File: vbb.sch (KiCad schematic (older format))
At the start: 24 parts, among them CON1 BARREL_JACK, J1 Screw_Terminal_1x02, P1 CONN_02X01, P3 CONN_02X04, P4 USB_B, P5 USB_B, P6 USB_B, P7 USB_A

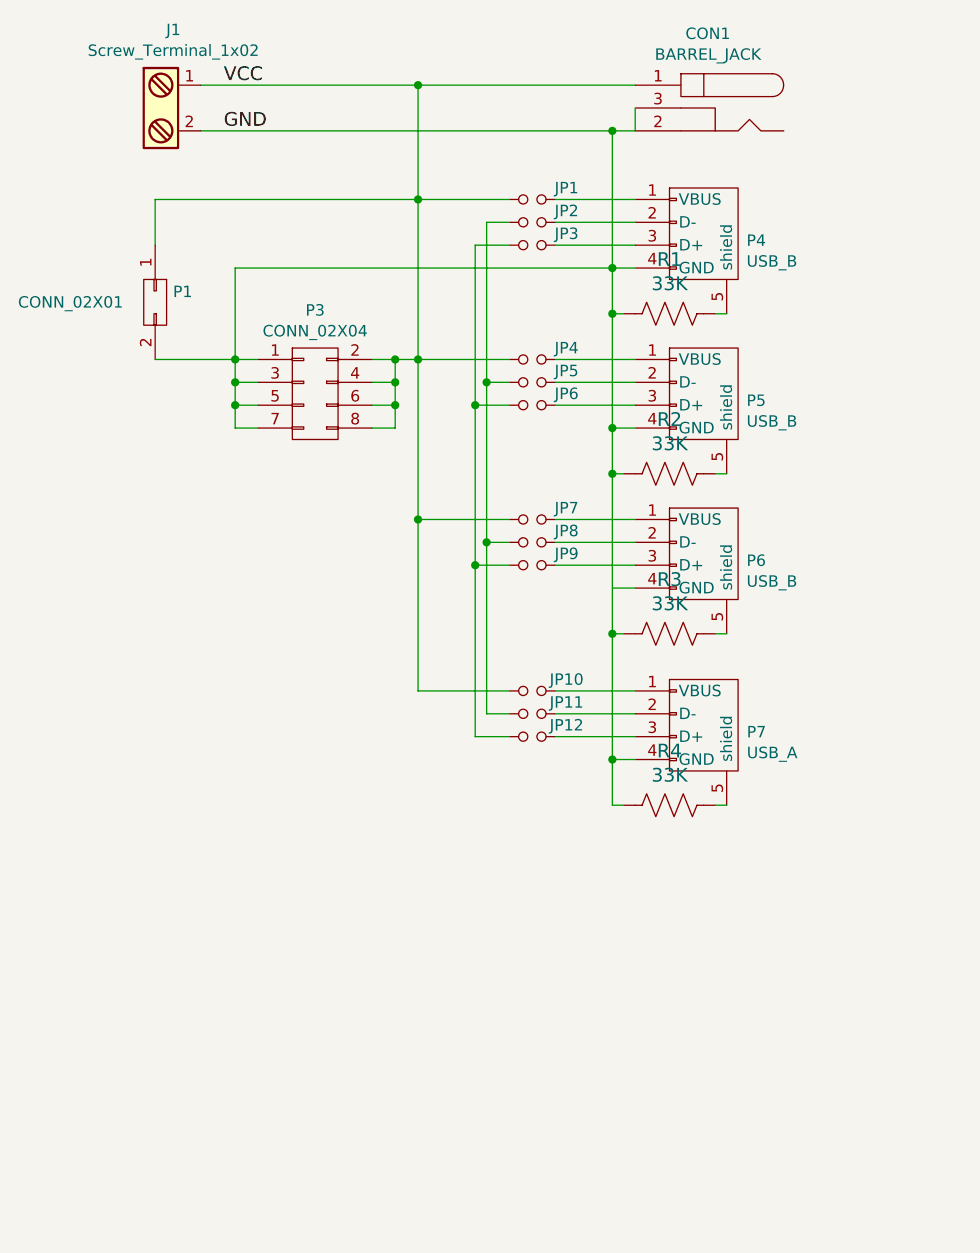
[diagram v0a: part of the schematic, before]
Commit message: Use Omron XM7D-0512 through hole USB mini connector
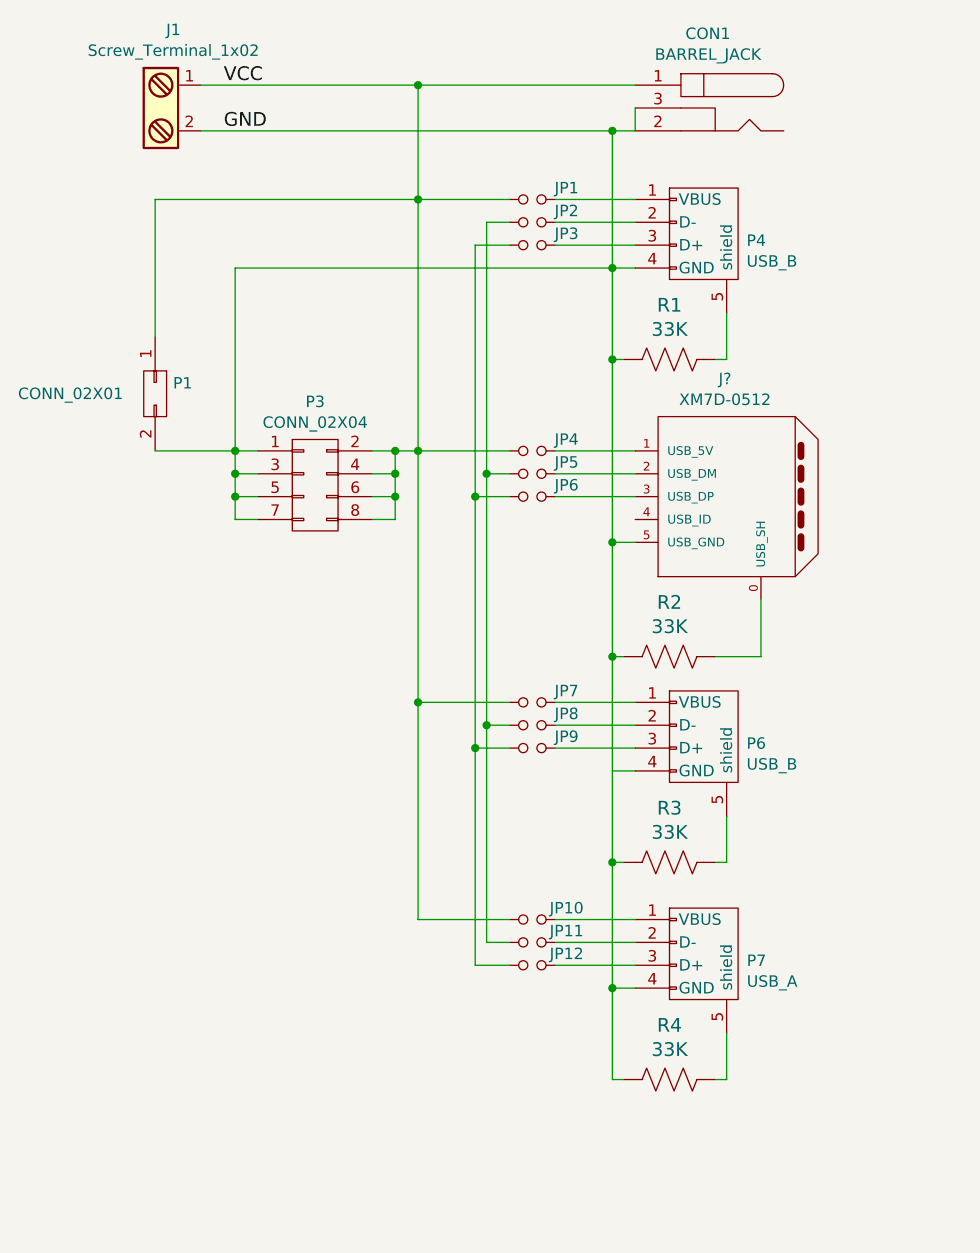
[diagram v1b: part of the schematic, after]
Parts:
- removed P5: USB_B, Connect:USB_Mini-B, symbol USB_B
- added J?: XM7D-0512, symbol XM7D-0512
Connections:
- net GND: now also J?.5 (USB_GND)
- net at JP4.2: now also J?.1 (USB_5V)
- net at JP5.2: now also J?.2 (USB_DM)
- net at JP6.2: now also J?.3 (USB_DP)
- net at R2.2 (K): now also J?.0 (USB_SH)
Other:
- moved on the sheet: JP10, JP11, JP12, JP4, JP5, JP6, JP7, JP8, JP9, P1, P3, P6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

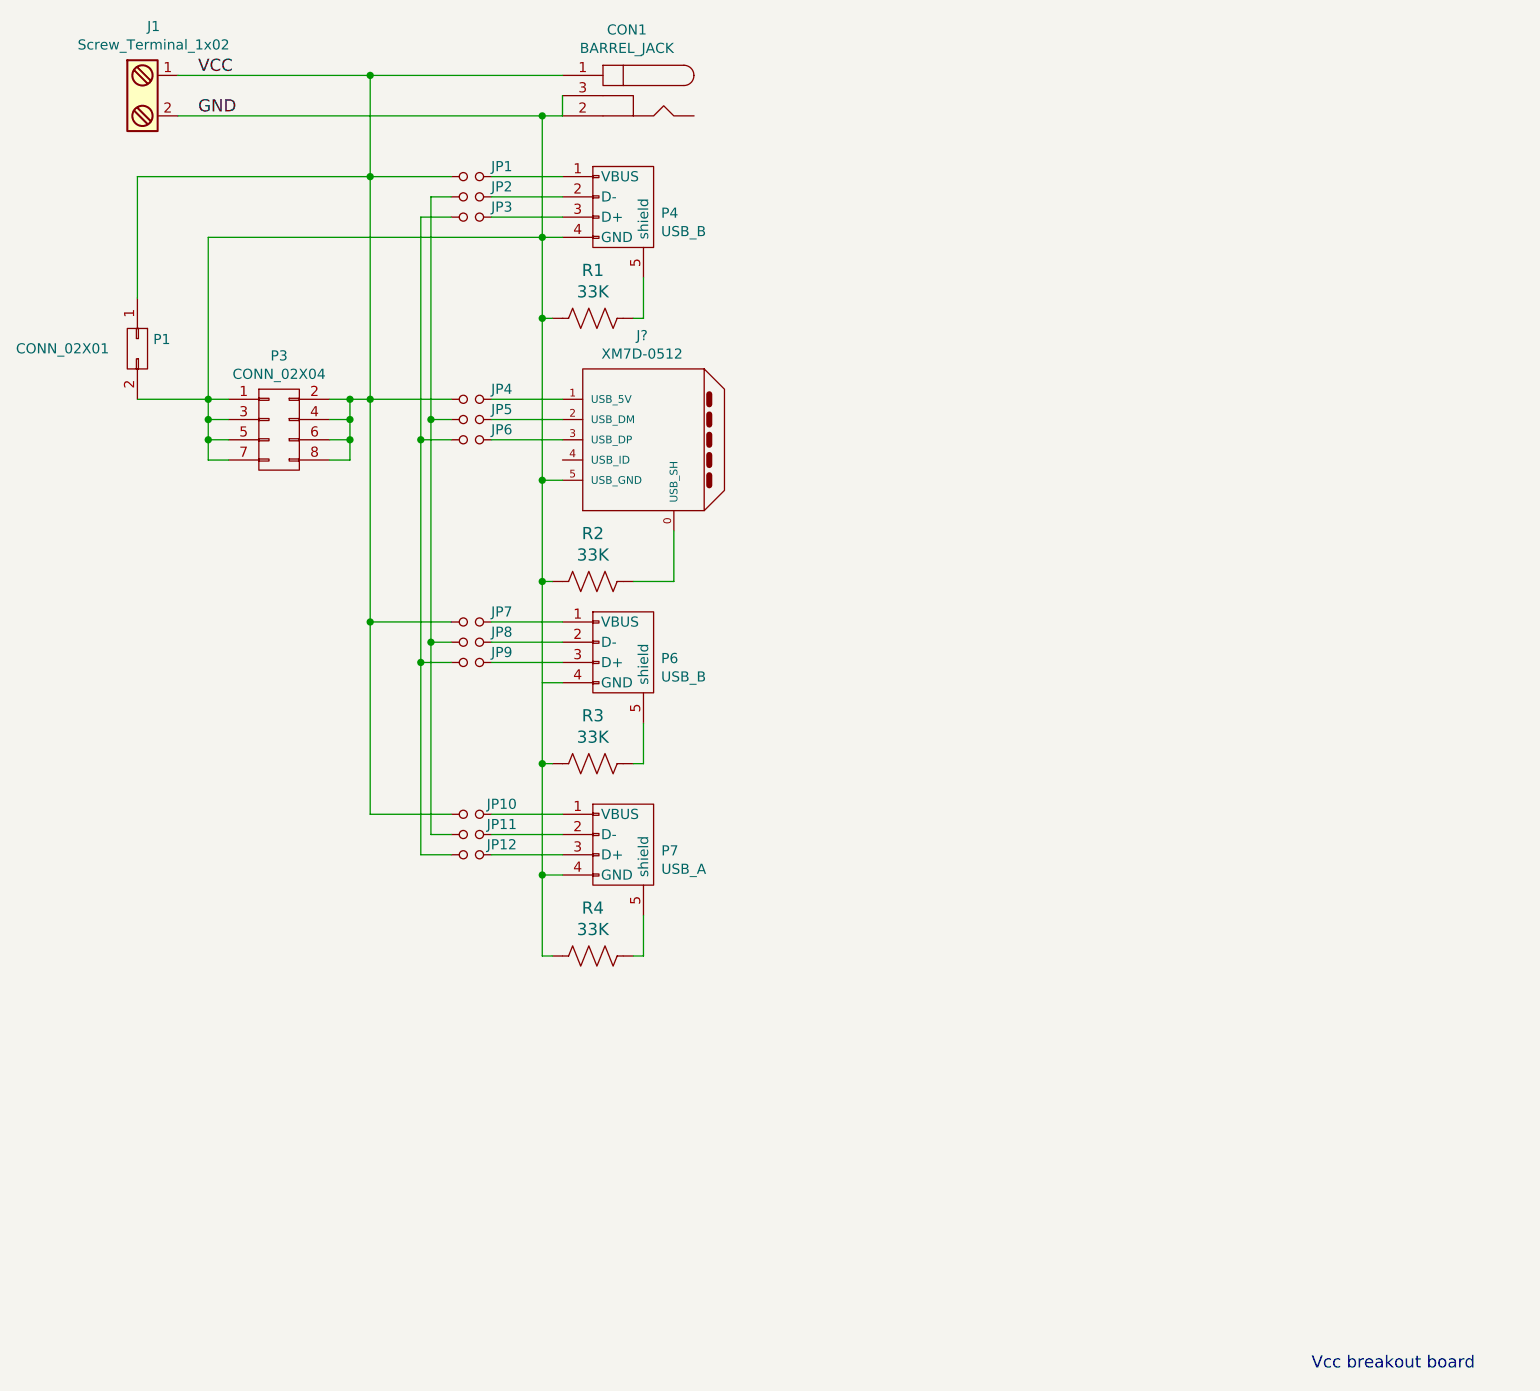
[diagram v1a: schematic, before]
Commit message: Combined separate jumpers into a 2x03 connector As a result, board now fits the 50mmx50mm size group.
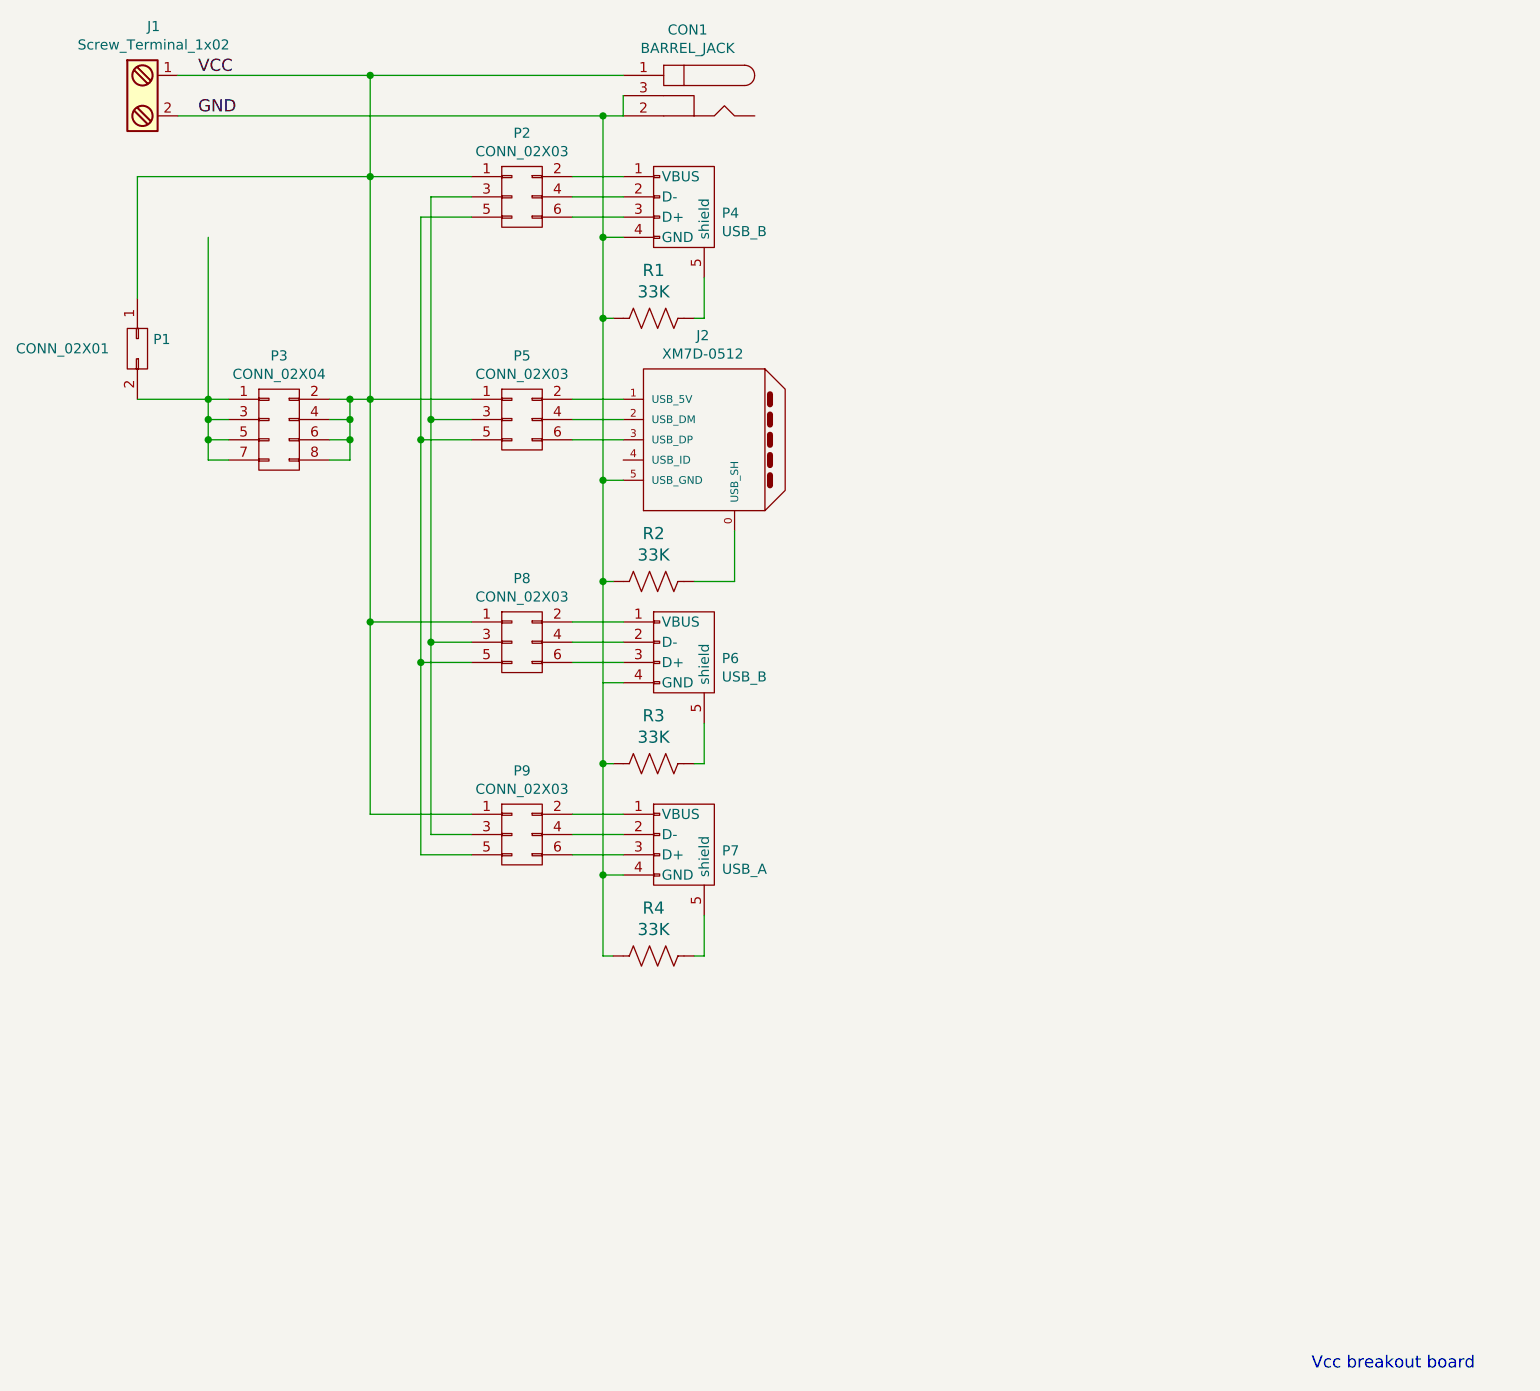
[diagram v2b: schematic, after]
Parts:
- removed JP1, JP10, JP11, JP12, JP2, JP3, JP4, JP5, JP6, JP7, JP8, JP9: JUMPER_NO_Small, Pin_Headers:Pin_Header_Straight_1x02, symbol JUMPER_NO_Small
- added P2, P5, P8, P9: CONN_02X03, Pin_Headers:Pin_Header_Straight_2x03, symbol CONN_02X03
- J2: renamed from J?; footprint (none) -> Omron:XM7D-0512
- P6: footprint Connect:USB_Micro-B -> w_conn_pc:conn_usb_B_micro_smd
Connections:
- net GND: no longer P1.2 (P2), P3.1 (P1), P3.3 (P3), P3.5 (P5), P3.7 (P7)
- net VCC: now also P2.1 (P1), P5.1 (P1), P8.1 (P1), P9.1 (P1)
- net at P7.1 (VBUS): now also P9.2 (P2)
- net at P7.2 (D-): now also P9.4 (P4)
- net at P7.3 (D+): now also P9.6 (P6)
- net at J2.1 (USB_5V): now also P5.2 (P2)
- net at J2.2 (USB_DM): now also P5.4 (P4)
- net at J2.3 (USB_DP): now also P5.6 (P6)
- net at P4.1 (VBUS): now also P2.2 (P2)
- net at P4.2 (D-): now also P2.4 (P4)
- net at P4.3 (D+): now also P2.6 (P6)
- net at P6.1 (VBUS): now also P8.2 (P2)
- net at P6.2 (D-): now also P8.4 (P4)
- net at P6.3 (D+): now also P8.6 (P6)
- new net: P1.2 (P2), P3.1 (P1), P3.3 (P3), P3.5 (P5), P3.7 (P7)
- new net: P2.3 (P3), P5.3 (P3), P8.3 (P3), P9.3 (P3)
- new net: P2.5 (P5), P5.5 (P5), P8.5 (P5), P9.5 (P5)
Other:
- moved on the sheet: CON1, J2, P4, P6, P7, R1, R2, R3, R4
